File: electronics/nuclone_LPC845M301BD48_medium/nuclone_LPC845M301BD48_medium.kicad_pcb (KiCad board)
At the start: 2 copper layers, 50 x 76.2 mm, 58 parts, among them J1 JTAG_2X05, J2 TYPE-C-31-M-12, J3 nuclone_medium_left, J4 nuclone_medium_right, J5 Conn_02x06_Odd_Even, SW1 RESET, SW2 Bootloader, U1 MCP1702-3.3V, U2 LPC845M301JBD48, U3 reference_sot23-3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

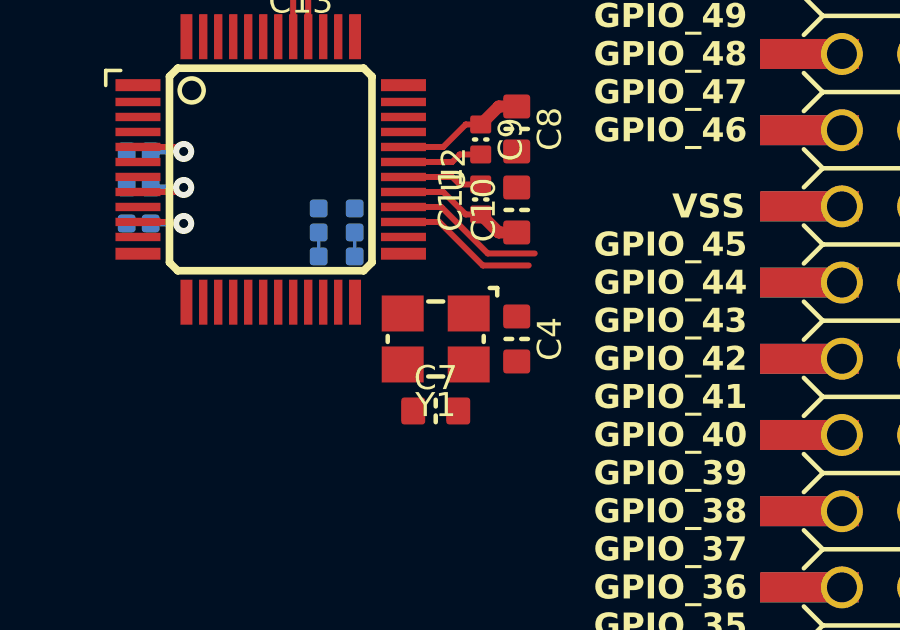
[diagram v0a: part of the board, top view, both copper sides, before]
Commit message: small routing and updated jumpers
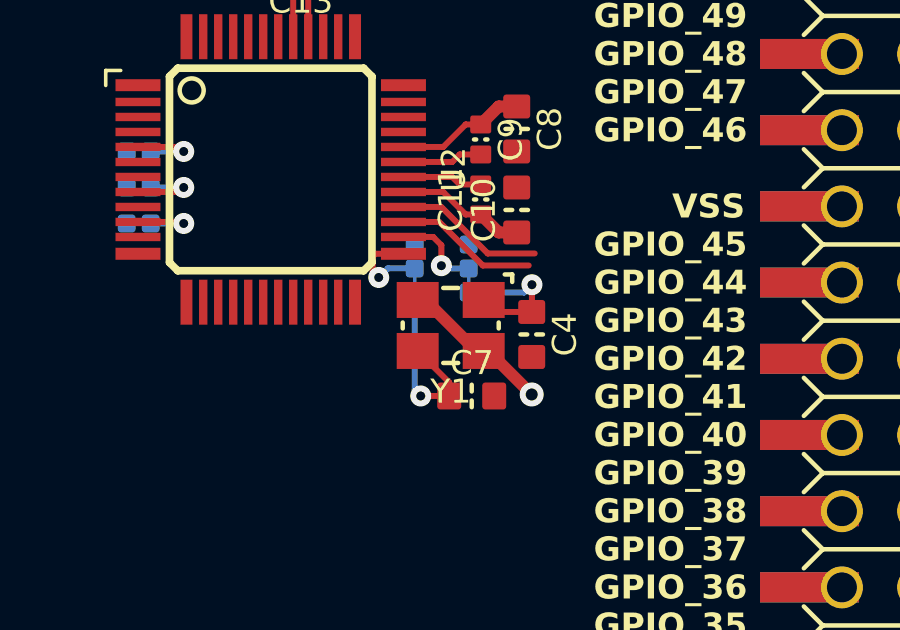
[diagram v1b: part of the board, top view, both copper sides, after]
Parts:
- moved JP6 3.98 mm to (61.6, 71.4)
- moved JP7 3.42 mm to (59.8, 71.4)
- moved C7 1.30 mm to (61.7, 75.7)
- moved Y1 0.67 mm to (61.0, 73.3)
- moved C4 0.52 mm to (63.7, 73.6)
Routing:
- net /microcontroller/XTALOUT: track 0.00 -> 6.42 mm, vias 0 -> 1
- net /VSS: track 44.9 -> 50.0 mm, vias 15 -> 16
- net /microcontroller/XTALIN: track 0.00 -> 4.89 mm, vias 0 -> 1
- net /microcontroller/PIO0_9_I: track 0.00 -> 3.07 mm, vias 0 -> 1
- net /microcontroller/PIO0_8_I: track 0.00 -> 3.01 mm, vias 0 -> 1

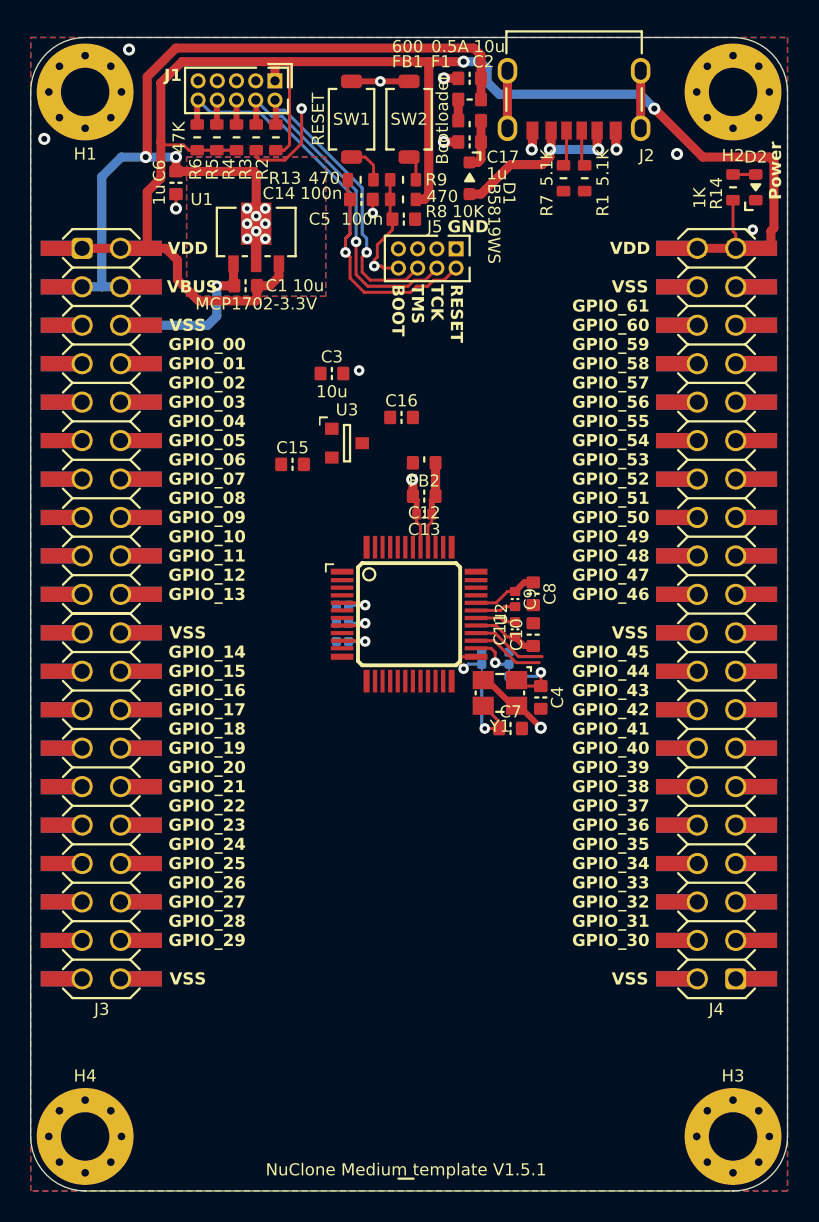
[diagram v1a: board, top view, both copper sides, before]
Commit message: place and route done, silk placement done, WIP relabeling
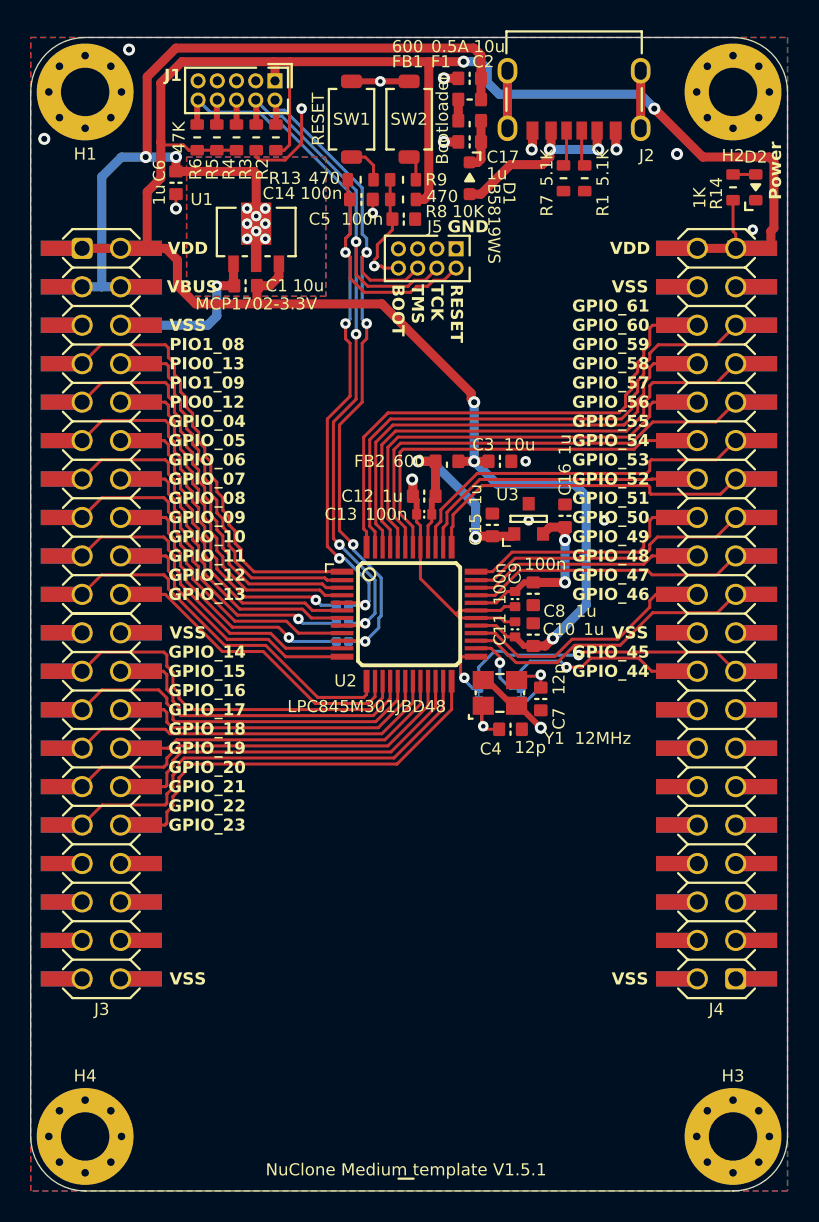
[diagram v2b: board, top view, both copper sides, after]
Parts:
- moved C15 13.8 mm to (60.5, 62.2), turned to 90 degrees
- moved U3 13.0 mm to (62.9, 61.8), turned to 90 degrees
- moved C16 12.6 mm to (65.3, 61.6), turned to 90 degrees
- moved C3 12.5 mm to (61.0, 58.0), turned to 180 degrees
- moved JP7 3.05 mm to (62.4, 73.0)
- moved C4 2.90 mm to (61.7, 75.7), turned to 0 degrees
- moved C7 2.79 mm to (63.7, 73.7), turned to -90 degrees
- moved JP6 2.56 mm to (59.6, 73.0)
- moved FB2 1.50 mm to (57.5, 58.0), turned to 0 degrees
- turned Y1 to 0 degrees
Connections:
- JP6 pad 2: /microcontroller/PIO0_8_I -> /microcontroller/PIO0_9_I
- JP7 pad 2: /microcontroller/PIO0_9_I -> /microcontroller/PIO0_8_I
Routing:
- net /VDD: track 113.6 -> 157.5 mm, vias 2 -> 5
- net /GPIO_60: track 0.00 -> 36.0 mm
- net /GPIO_61: track 0.00 -> 33.5 mm
- net /GPIO_58: track 0.00 -> 33.5 mm
- net /GPIO_59: track 0.00 -> 30.7 mm
- net /GPIO_56: track 0.00 -> 30.6 mm
- net /GPIO_22: track 0.00 -> 29.9 mm
- net /GPIO_00: track 0.00 -> 29.3 mm
- net /TMS: track 22.9 -> 51.1 mm, vias 2 -> 4
- net /GPIO_57: track 0.00 -> 27.9 mm
- net /GPIO_02: track 0.00 -> 27.9 mm
- net /GPIO_23: track 0.00 -> 27.3 mm
- net /TCK: track 25.1 -> 52.4 mm, vias 2 -> 4
- net /GPIO_20: track 0.00 -> 26.9 mm
- net /GPIO_04: track 0.00 -> 26.2 mm, vias 0 -> 1
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
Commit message: labels done, keepout around crystal
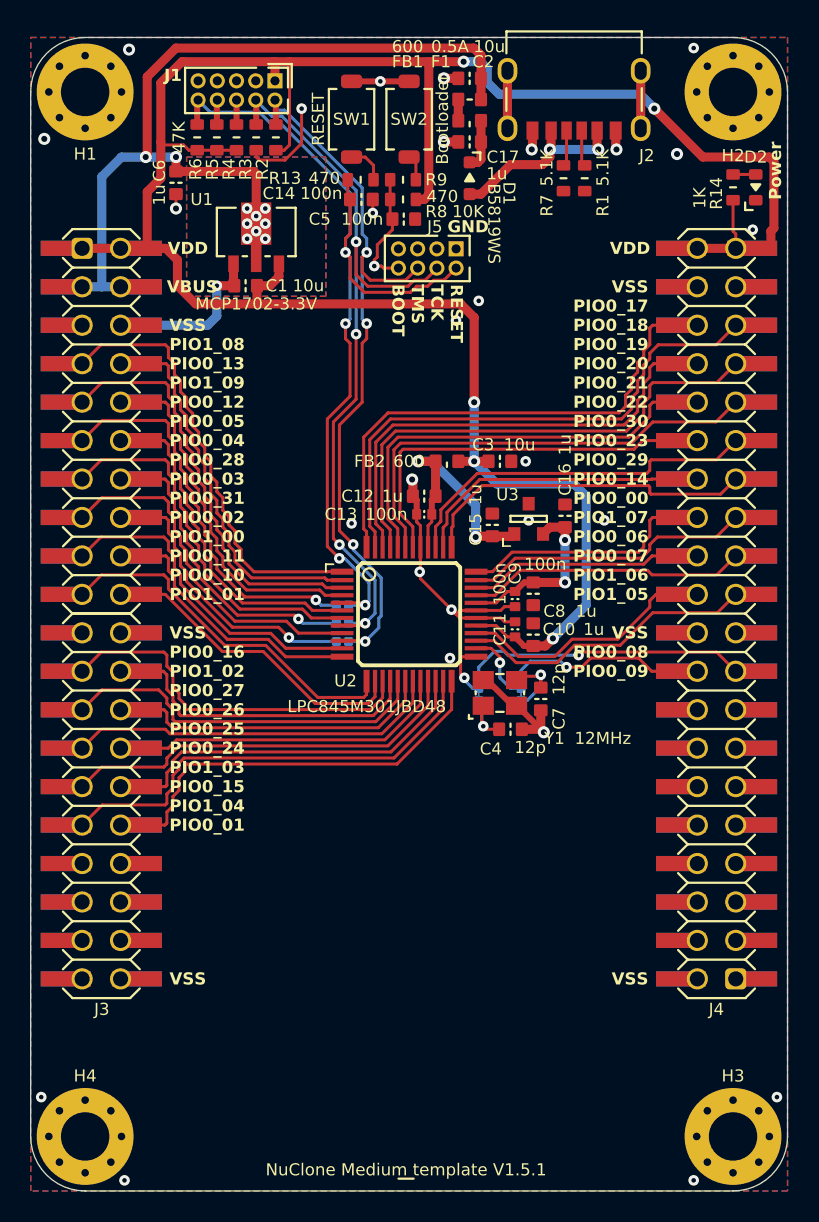
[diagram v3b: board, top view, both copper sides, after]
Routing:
- net /VSS: track 58.2 -> 61.4 mm, vias 18 -> 29
- net /VDD: track 157.5 -> 160.5 mm

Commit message: updated versions, fixed DRC's
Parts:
- N2: value V20240606 -> V20240628
- N5: value Nuclone Template V20240606 -> Nuclone LPC845 LQFP48
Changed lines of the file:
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@@
         (effects (font (size 1 1) (thickness 0.15)) (justify mirror))
     )
-    (fp_text value "V20240606" (at -0.05 0.1) (layer "B.SilkS")
+    (fp_text value "V20240628" (at -0.05 0.1) (layer "B.SilkS")
         (effects (font (size 0.8 0.8) (thickness 0.15)) (justify mirror))
     )
@@
         (effects (font (size 1 1) (thickness 0.15)) (justify mirror))
     )
-    (fp_text value "Nuclone Template V20240606" (at 0.8 0.23) (layer "B.SilkS")
+    (fp_text value "Nuclone LPC845 LQFP48" (at 0.8 0.23) (layer "B.SilkS")
         (effects (font (size 0.8 0.8) (thickness 0.15)) (justify mirror))
     )
@@
     (property "Sheetname" "microcontroller")
     (net_tie_pad_groups "1, 2")
-    (fp_text reference "JP6" (at 0 1.1 270) (layer "B.SilkS")
-        (effects (font (size 0.8 0.8) (thickness 0.15)) (justify mirror))
-    )
-    (fp_text value "PIO_8/XTAL" (at 0 -1.1 270) (layer "B.SilkS")
+    (fp_text reference "JP6" (at 0 1.1 270) (layer "B.SilkS") hide
+        (effects (font (size 0.8 0.8) (thickness 0.15)) (justify mirror))
+    )
+    (fp_text value "PIO_8/XTAL" (at 4.9 0 270) (layer "B.SilkS")
         (effects (font (size 0.8 0.8) (thickness 0.15) bold) (justify mirror))
     )
@@
     (property "Sheetname" "microcontroller")
     (net_tie_pad_groups "1, 2")
-    (fp_text reference "JP7" (at 0.1 1.2 270) (layer "B.SilkS")
-        (effects (font (size 0.8 0.8) (thickness 0.15)) (justify mirror))
-    )
-    (fp_text value "PIO_9/XTAL" (at 0 -1.1 270) (layer "B.SilkS")
+    (fp_text reference "JP7" (at 0.1 1.2 270) (layer "B.SilkS") hide
+        (effects (font (size 0.8 0.8) (thickness 0.15)) (justify mirror))
+    )
+    (fp_text value "PIO_9/XTAL" (at 4.9 0 270) (layer "B.SilkS")
         (effects (font (size 0.8 0.8) (thickness 0.15) bold) (justify mirror))
     )
@@
     (property "Sheetname" "microcontroller")
     (attr smd)
-    (fp_text reference "JP3" (at 0 1.1) (layer "B.SilkS")
-        (effects (font (size 0.8 0.8) (thickness 0.15)) (justify mirror))
-    )
-    (fp_text value "PIO0_2" (at 0 -1.1) (layer "B.SilkS")
+    (fp_text reference "JP3" (at 0 1.1) (layer "B.SilkS") hide
+        (effects (font (size 0.8 0.8) (thickness 0.15)) (justify mirror))
+    )
+    (fp_text value "PIO0_2" (at 3.1 -0.1) (layer "B.SilkS")
         (effects (font (size 0.8 0.8) (thickness 0.15) bold) (justify mirror))
     )
@@
     (property "Sheetname" "microcontroller")
     (attr smd)
-    (fp_text reference "JP5" (at 0 1.1) (layer "B.SilkS")
-        (effects (font (size 0.8 0.8) (thickness 0.15)) (justify mirror))
-    )
-    (fp_text value "PIO0_5" (at 0 -1.1) (layer "B.SilkS")
+    (fp_text reference "JP5" (at 0 1.1) (layer "B.SilkS") hide
+        (effects (font (size 0.8 0.8) (thickness 0.15)) (justify mirror))
+    )
+    (fp_text value "PIO0_5" (at 3.1 0) (layer "B.SilkS")
         (effects (font (size 0.8 0.8) (thickness 0.15) bold) (justify mirror))
     )
@@
     (property "Sheetname" "microcontroller")
     (attr smd)
-    (fp_text reference "JP4" (at 0 1.1) (layer "B.SilkS")
-        (effects (font (size 0.8 0.8) (thickness 0.15)) (justify mirror))
-    )
-    (fp_text value "PIO0_3" (at 0 -1.1) (layer "B.SilkS")
+    (fp_text reference "JP4" (at 0 1.1) (layer "B.SilkS") hide
+        (effects (font (size 0.8 0.8) (thickness 0.15)) (justify mirror))
+    )
+    (fp_text value "PIO0_3" (at 3.1 0) (layer "B.SilkS")
         (effects (font (size 0.8 0.8) (thickness 0.15) bold) (justify mirror))
     )

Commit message: minor changes
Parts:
- N4: value NuClone Medium template V1.5.1 -> NuClone LPC845 PQFP48
- N5: value Nuclone LPC845 LQFP48 -> Nuclone Template V20240606
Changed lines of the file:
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@@
         (effects (font (size 1 1) (thickness 0.15)))
     )
-    (fp_text value "NuClone Medium template V1.5.1" (at 0 0.0125) (layer "F.SilkS")
+    (fp_text value "NuClone LPC845 PQFP48" (at 0 0.0125) (layer "F.SilkS")
         (effects (font (size 0.8 0.8) (thickness 0.15)))
     )
@@
         (effects (font (size 1 1) (thickness 0.15)) (justify mirror))
     )
-    (fp_text value "Nuclone LPC845 LQFP48" (at 0.8 0.23) (layer "B.SilkS")
+    (fp_text value "Nuclone Template V20240606" (at 0.8 0.23) (layer "B.SilkS")
         (effects (font (size 0.8 0.8) (thickness 0.15)) (justify mirror))
     )

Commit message: added boot button jumper
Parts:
- added JP1: BOOT, SquantorSpecial:solder_jumper_0402_2way_noconn, B.Cu at (53.9, 65.6)
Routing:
- net /Bootloader: track 7.91 -> 31.8 mm, vias 1 -> 3
- net /GPIO_03: track 23.0 -> 27.1 mm, vias 0 -> 1
- net /RESET: track 61.6 -> 63.1 mm
- net /TCK: track 52.4 -> 53.7 mm
- net /TMS: track 51.1 -> 51.9 mm
- net /microcontroller/VDDA: track 16.7 -> 16.1 mm
- net /VSS: vias 29 -> 30

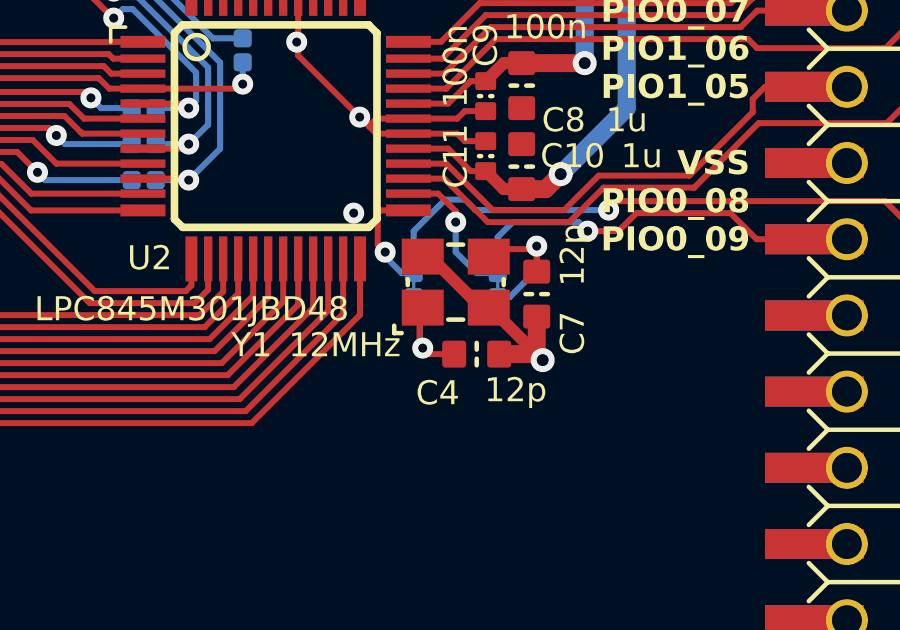
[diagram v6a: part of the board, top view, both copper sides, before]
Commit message: easier to solder crystal
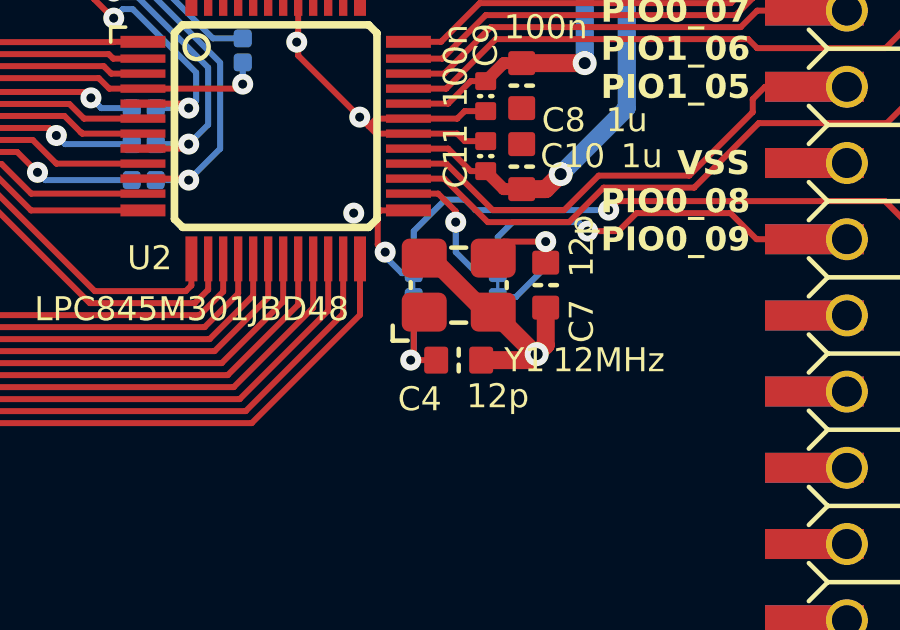
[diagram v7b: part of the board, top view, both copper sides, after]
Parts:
- Y1: footprint SquantorCrystal:Crystal_3225_4 -> SquantorCrystal:Crystal_3225_4_hand
- moved C4 0.63 mm to (61.1, 75.9)
- moved C7 0.42 mm to (64.0, 73.4)
- moved Y1 0.14 mm to (61.1, 73.4)
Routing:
- net /microcontroller/XTALIN: track 4.39 -> 4.91 mm

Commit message: prepped for production with updated versionnumbers and some minor changes
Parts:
- N2: value V20240628 -> V20240712
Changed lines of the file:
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@@
         (effects (font (size 1 1) (thickness 0.15)) (justify mirror))
     )
-    (fp_text value "V20240628" (at -0.05 0.1) (layer "B.SilkS")
+    (fp_text value "V20240712" (at -0.05 0.1) (layer "B.SilkS")
         (effects (font (size 0.8 0.8) (thickness 0.15)) (justify mirror))
     )
